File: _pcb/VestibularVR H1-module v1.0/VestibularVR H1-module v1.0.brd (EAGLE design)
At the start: 43 x 56.5 mm, 70 parts, among them IC1 FT232RL, IC2 74LVC1G07DBV, IC3 TLV70033DDCR, IC4 74LVC1G07DBV, IC5 74LVC1G07DBV, IC6 74LVC1G07DBV, IC7 USBLC6-2SC6, IC8 ATXMEGA32A4U, X1 TSW-105-02-S-D, X2 TSW-105-02-S-D, X7 22-23-2051

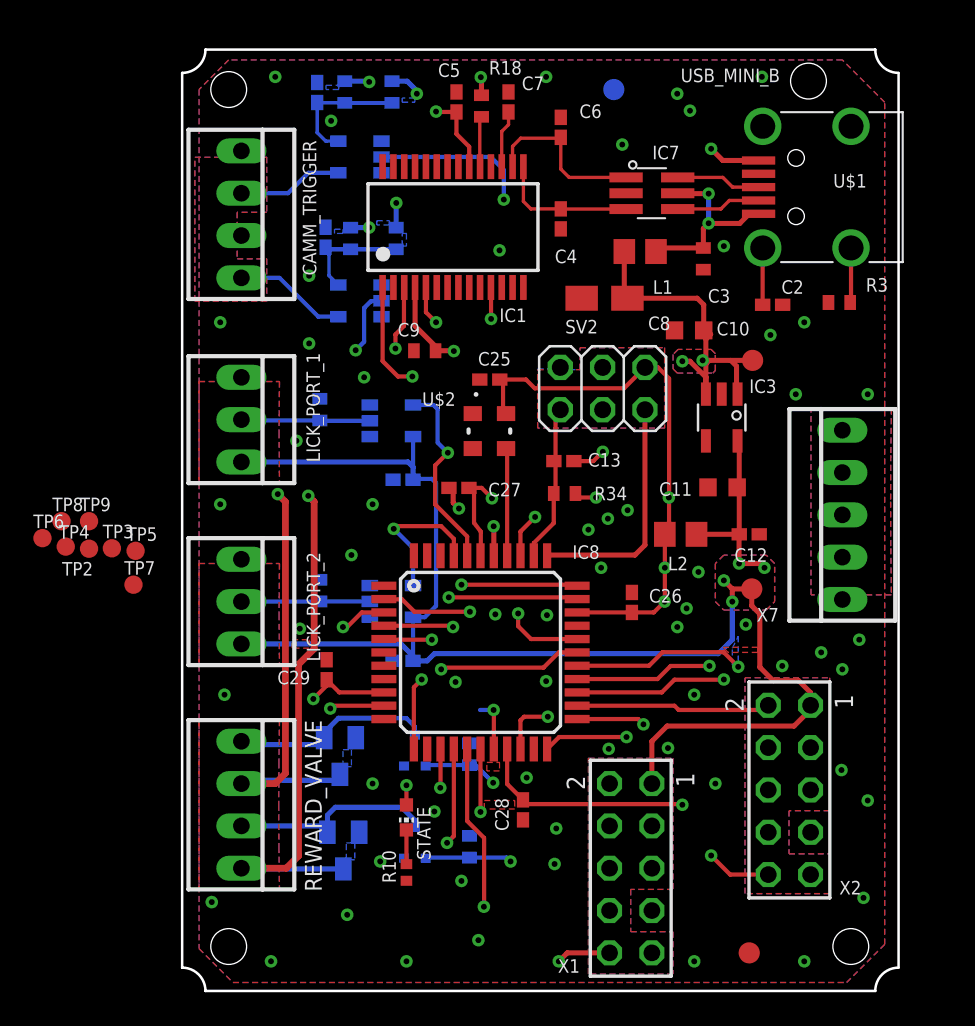
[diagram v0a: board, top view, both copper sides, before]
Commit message: v.1.0 pcb design as finished; still missing to hear about it from Filipe
. David's pcb v.1.0 design as finished
  - mechanical holes final tuning
  - main labels final design
. still missing to hear about it from Filipe
. next step - building BOM
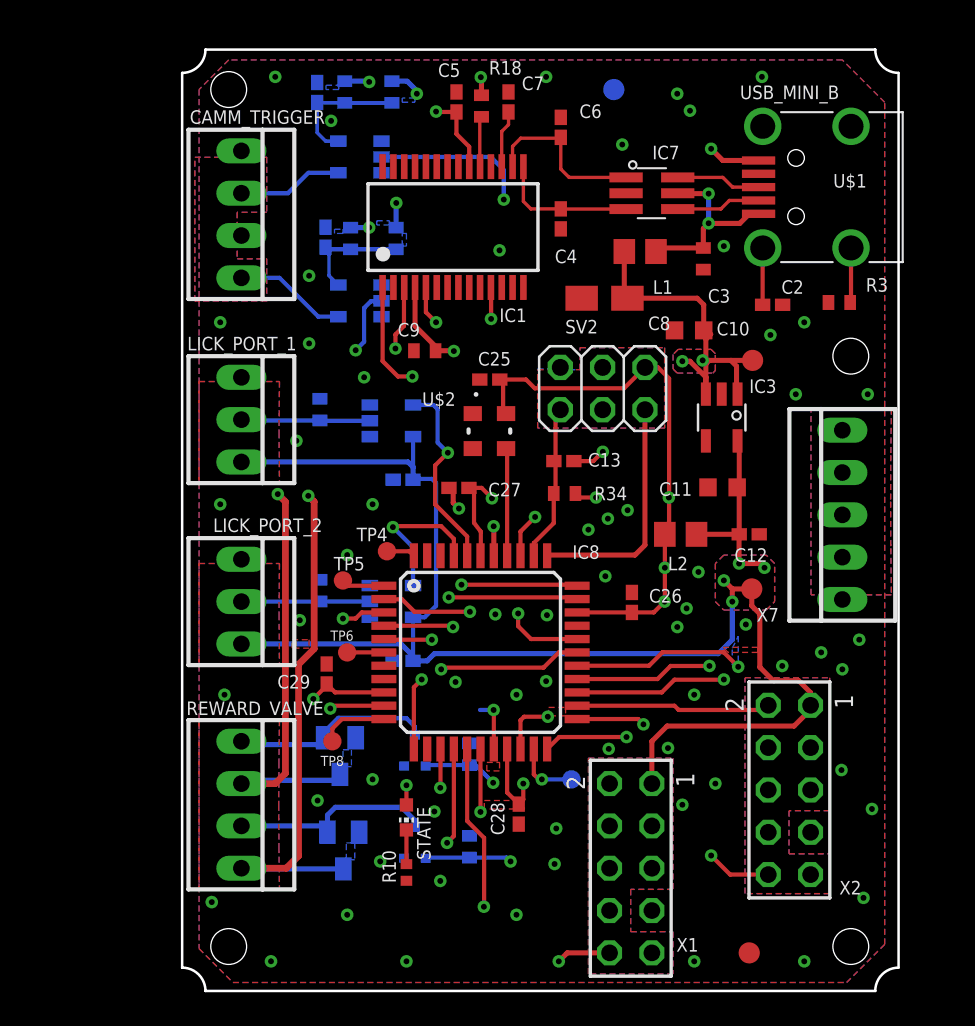
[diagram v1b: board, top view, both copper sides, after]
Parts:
- removed TP2, TP3, TP7: WIREPADSMD1,27-254, testpad:TP11R
- moved TP9 32.8 mm to (23.4, 12.7), flipped to the bottom
- moved TP8 20.9 mm to (9.02, 15.0)
- moved TP6 19.5 mm to (9.91, 20.3)
- moved TP4 17.9 mm to (12.3, 26.4)
- moved TP5 12.6 mm to (9.65, 24.6)
- moved C28 0.36 mm to (20.2, 10.6)
- moved C29 0.25 mm to (8.68, 19.0)
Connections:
- removed net N$10: IC8.43, TP3.TP
- removed net N$15: IC8.7, TP7.TP
- removed net N$8: IC8.42, TP2.TP
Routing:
- net N$17: track 0.00 -> 4.09 mm
- net N$18: track 0.00 -> 3.91 mm, vias 0 -> 1
- net +3V3_U: track 113.5 -> 110.9 mm, vias 8 -> 10
- net N$12: track 0.00 -> 2.59 mm
- net N$13: track 0.00 -> 2.20 mm
- net N$11: track 0.00 -> 1.73 mm
- net U_OPTICAL_FLOW_2_INT: track 43.8 -> 44.4 mm
- added copper zone on layer 1, net N$15

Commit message: final versions committed & CAM data
VestibularVR H1-module v1.0
  &
Lick Sensor module v1.0
final versions committed !!!

.created CAM data for both boards
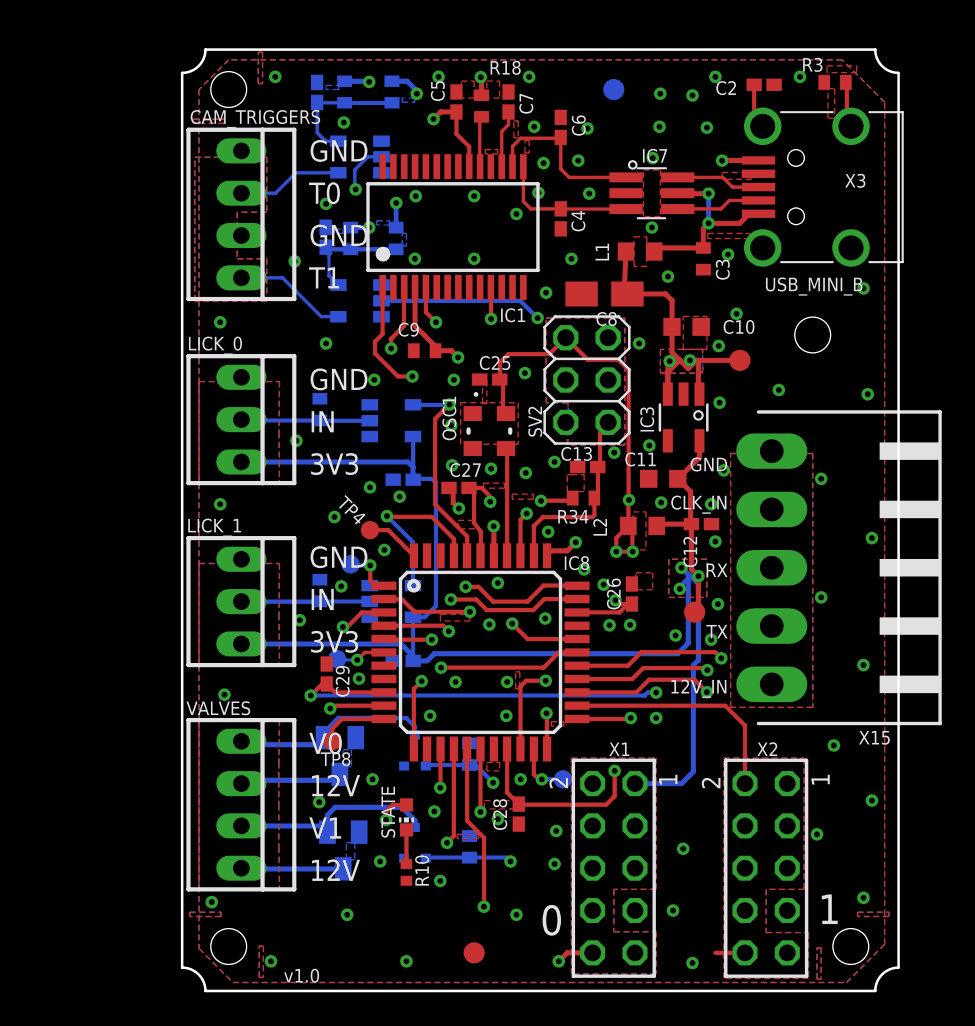
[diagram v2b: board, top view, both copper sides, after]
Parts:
- removed X7: 22-23-2051, con-molex:22-23-2051
- added X15: (no value), con-weidmueller-sl35:90G-5
- L1, L2: device rcl:R0805 -> rcl:R0603
- moved TP10 16.5 mm to (17.5, 2.29)
- moved C2 13.2 mm to (34.9, 54.4)
- moved R3 13.2 mm to (39.2, 54.5)
- moved X2 4.90 mm to (35.1, 7.37)
- moved TP1 3.70 mm to (30.8, 22.7)
- moved C11 3.59 mm to (28.9, 30.7)
- moved C12 2.93 mm to (31.2, 28.0)
- moved L2 2.34 mm to (27.6, 27.9)
- moved IC3 2.29 mm to (30.1, 34.4)
- moved TP4 1.63 mm to (11.3, 27.7)
- moved C13 1.48 mm to (24.3, 31.4), turned to 180 degrees
- moved R34 1.17 mm to (24.1, 29.6), turned to 180 degrees
- moved SV2 1.07 mm to (24.3, 36.7), turned to 90 degrees
- moved TP5 1.07 mm to (10.1, 25.6), flipped to the bottom
- moved X1 1.02 mm to (25.9, 7.37)
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- renumbered CAMM_TRIGGER to CAM_TRIGGERS, LICK_PORT_1 to LICK_0, LICK_PORT_2 to LICK_1, REWARD_VALVE to VALVES, U$1 to X3, U$2 to OSC1, U$4 to T2, U$7 to T1
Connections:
- removed net N$59: C2.1, X3.SHIELD_4
- new net N$15: C2.1, X3.SHIELD_3
- net +12V: now also X15.1; no longer X7.5
- net GND: now also X15.5; no longer X7.1
- net HARP_H1_BOARD_RX: now also X15.3; no longer X7.3
- net HARP_H1_BOARD_TX: now also X15.2; no longer X7.4
- net HARP_H1_CLOCK_IN: now also X15.4; no longer X7.2
- net N$1: now also X3.SHIELD_2; no longer X3.SHIELD_1
- net U_CAM1_TRIGGER: now also IC4.2; no longer IC2.2
- net U_CAM2_TRIGGER: now also IC2.2; no longer IC4.2
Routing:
- net +12V: track 127.5 -> 87.6 mm, vias 2 -> 0
- net HARP_H1_BOARD_TX: track 31.2 -> 17.7 mm
- net HARP_H1_BOARD_RX: track 33.1 -> 23.7 mm
- net GND: track 18.7 -> 9.47 mm, vias 55 -> 96
- net U_CAM1_TRIGGER: track 29.4 -> 38.3 mm
- net +3V3: track 209.5 -> 200.7 mm, vias 10 -> 9
- net U_OPTICAL_FLOW_2_INT: track 44.4 -> 36.7 mm
- net U_CAM2_TRIGGER: track 45.6 -> 38.0 mm
- net U_OPTICAL_FLOW_2_MISO: track 20.5 -> 24.5 mm
- net U_OPTICAL_FLOW_2_SCK: track 18.6 -> 22.0 mm
- net N$59: track 3.41 -> 0.00 mm
- net U_OPTICAL_FLOW_2_MOSI: track 15.4 -> 18.3 mm
- net N$15: track 0.00 -> 2.71 mm
- net +3V3_U: track 110.9 -> 108.3 mm, vias 10 -> 9
- net PDI_CLK: track 9.51 -> 12.1 mm
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- added copper zone on layer 1, net N$10
- added copper zone on layer 15, net N$100
- added copper zone on layer 1, net N$101
- added copper zone on layer 1, net N$102
- added copper zone on layer 2, net N$103
- added copper zone on layer 15, net N$104
- added copper zone on layer 16, net N$105
- added copper zone on layer 1, net N$106
- added copper zone on layer 1, net N$107
- added copper zone on layer 1, net N$108
- added copper zone on layer 15, net N$109
- added copper zone on layer 15, net N$110
- added copper zone on layer 15, net N$111
- added copper zone on layer 1, net N$16
- added copper zone on layer 1, net N$24
- added copper zone on layer 1, net N$25
- added copper zone on layer 1, net N$26
- added copper zone on layer 1, net N$27
- added copper zone on layer 1, net N$45
- added copper zone on layer 1, net N$47
- added copper zone on layer 1, net N$48
- added copper zone on layer 1, net N$55
- added copper zone on layer 1, net N$57
- added copper zone on layer 1, net N$59
- added copper zone on layer 1, net N$69
- added copper zone on layer 1, net N$7
- added copper zone on layer 1, net N$70
- added copper zone on layer 1, net N$71
- added copper zone on layer 2, net N$72
- added copper zone on layer 15, net N$73
- added copper zone on layer 16, net N$74
- added copper zone on layer 1, net N$75
- added copper zone on layer 1, net N$76
- added copper zone on layer 1, net N$77
- added copper zone on layer 15, net N$78
- added copper zone on layer 2, net N$79
- added copper zone on layer 15, net N$80
- added copper zone on layer 16, net N$81
- added copper zone on layer 1, net N$82
- added copper zone on layer 2, net N$83
- added copper zone on layer 15, net N$84
- added copper zone on layer 16, net N$85
- added copper zone on layer 1, net N$86
- added copper zone on layer 2, net N$87
- added copper zone on layer 15, net N$88
- added copper zone on layer 16, net N$89
- added copper zone on layer 1, net N$90
- added copper zone on layer 2, net N$91
- added copper zone on layer 15, net N$92
- added copper zone on layer 16, net N$93
- added copper zone on layer 1, net N$94
- added copper zone on layer 2, net N$95
- added copper zone on layer 15, net N$96
- added copper zone on layer 16, net N$97
- added copper zone on layer 15, net N$98
- added copper zone on layer 15, net N$99
- removed copper zone on layer 1, net N$15
- removed copper zone on layer 2, net N$45
- removed copper zone on layer 15, net N$47
- removed copper zone on layer 16, net N$48
- removed copper zone on layer 2, net N$55
- removed copper zone on layer 16, net N$57
- removed copper zone on layer 2, net N$69
- removed copper zone on layer 2, net N$7
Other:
- board text added: "0"
- board text added: "1"
- board text added: "12V"
- board text added: "12V_IN"
- board text added: "3V3"
- board text added: "CLK_IN"
- board text added: "GND"
- board text added: "IN"
- board text added: "RX"
- board text added: "T0"
- board text added: "T1"
- board text added: "TX"
- board text added: "V0"
- board text added: "V1"
- board text added: "v1.0"
- board text removed: "Vestibular VR H1 Module"

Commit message: tunings on last versions
tunings on last versions:
  - labels size & positions
  - VestibularVR H1 module get 1mm more height
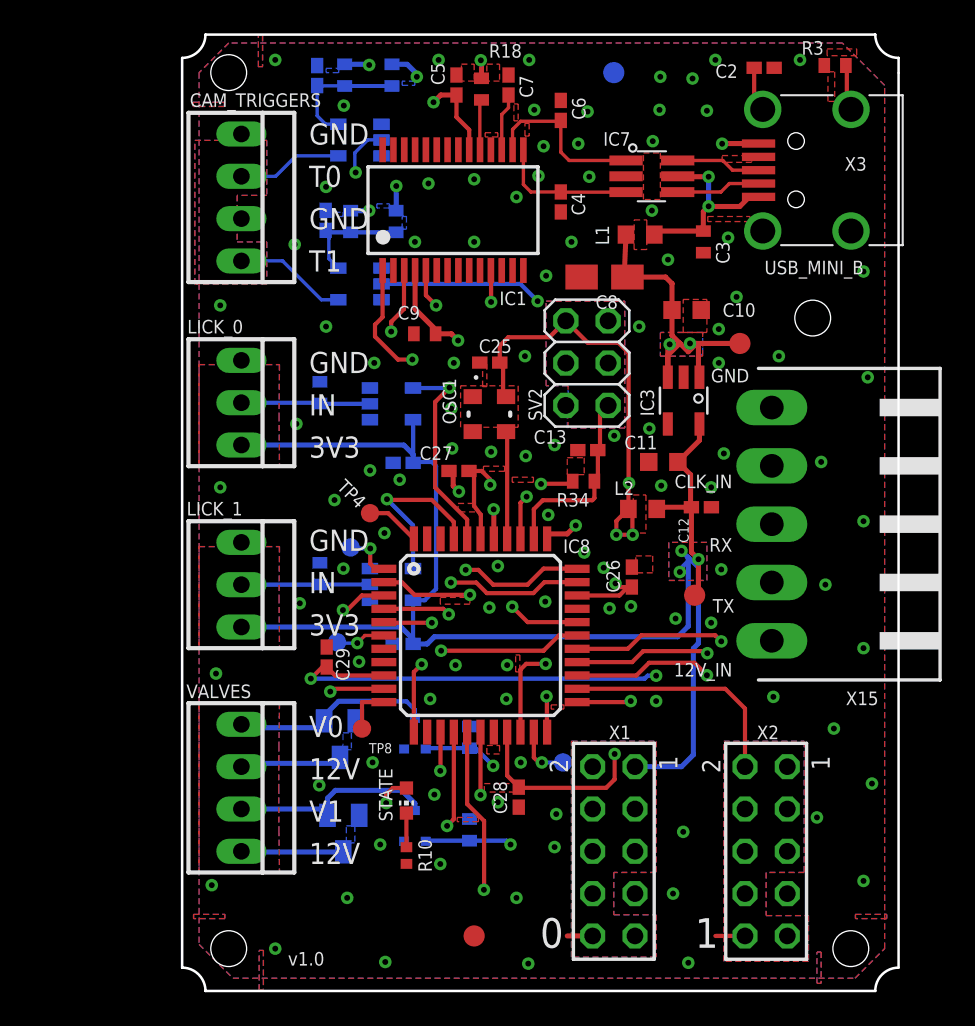
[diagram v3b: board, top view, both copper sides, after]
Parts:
- moved X15 2.62 mm to (40.6, 28.0)
- moved TP8 1.93 mm to (10.8, 15.7)
- moved C25 1.02 mm to (18.5, 37.7)
- moved C3 1.02 mm to (31.3, 45.0)
- moved IC4 1.02 mm to (10.7, 51.1)
- moved IC7 1.02 mm to (28.2, 48.9)
- moved L1 1.02 mm to (27.5, 45.4)
- moved R9 1.02 mm to (8.27, 35.9)
- moved TP11 1.02 mm to (25.9, 55.1)
- moved TP13 1.02 mm to (33.5, 38.9)
- moved X3 1.02 mm to (43.2, 49.3)
- moved C27 1.02 mm to (16.6, 31.2)
- moved C29 1.02 mm to (8.68, 20.0)
- moved IC5 1.02 mm to (12.6, 24.4)
- moved LICK_1 1.02 mm to (3.56, 24.4)
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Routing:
- net +12V: track 87.6 -> 90.7 mm
- net N$17: track 4.09 -> 2.90 mm
- net GND: track 9.47 -> 8.75 mm
- net +3V3: track 200.7 -> 200.1 mm
- added copper zone on layer 2, net N$102
- removed copper zone on layer 1, net N$102
- removed copper zone on layer 2, net N$103
- removed copper zone on layer 15, net N$104
- removed copper zone on layer 16, net N$105
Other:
- board size 43 x 56.5 mm -> 43 x 57.4 mm

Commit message: BOMs building
. BOMs building:
  - for both projects - Lick Sensor Module v1.0 & VestibularVR H1 Module v1.0
  - schm files modified (components parameters updated)

. Removed old Auxiliary Designs
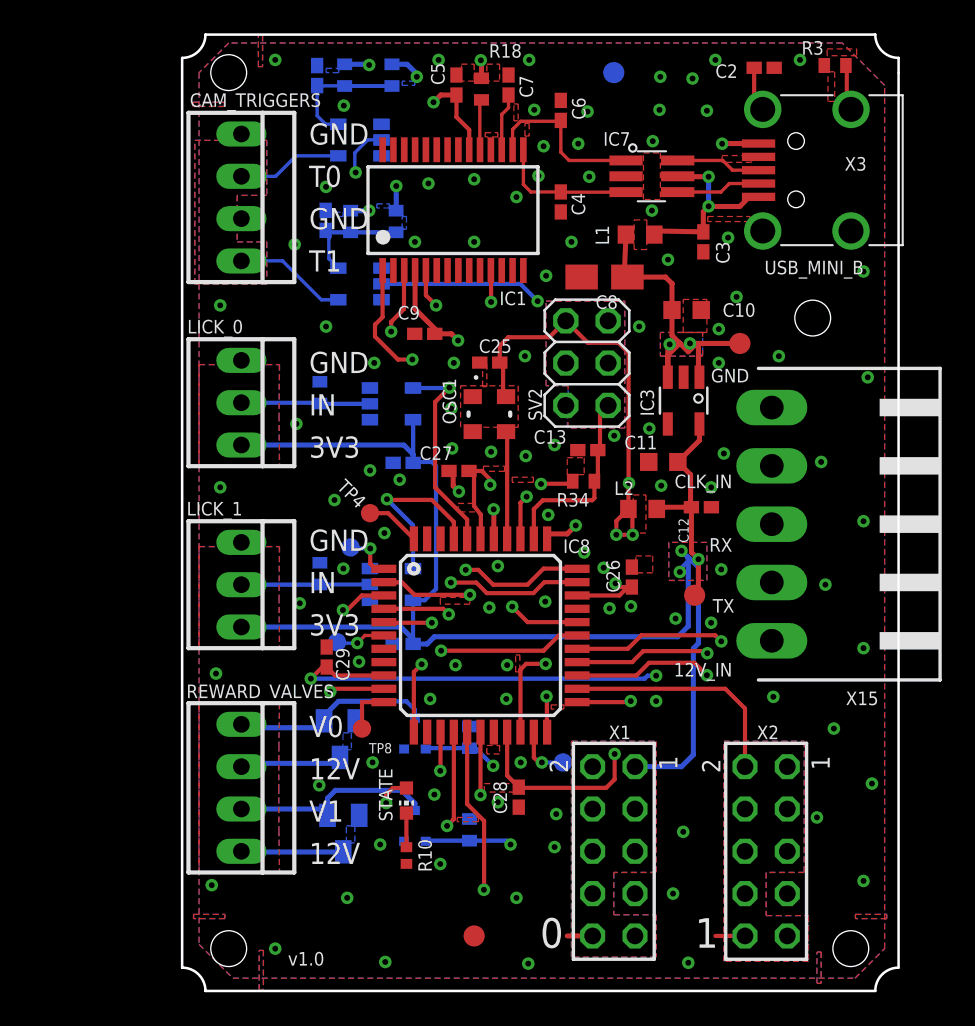
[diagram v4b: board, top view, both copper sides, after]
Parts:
- C3, C9: device rcl:C0402 -> rcl:C0402K
- R1, R5: value 0R DNI -> 0R
- R10: value 910 -> 330R
- R2, R6: value 0R DNI -> DNI
- STATE: value (none) -> GREEN_LED
- TP1, TP10, TP11, TP13: value TPB1,27 -> NO_COMPONENT
- TP4, TP5, TP6, TP8, TP9: value WIREPADSMD1,27-254 -> NO_COMPONENT
- X15: value (none) -> Main_plug
- renumbered VALVES to REWARD_VALVES

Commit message: BOM being updated
BOM being updated
not yet finished
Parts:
- C8: device rcl:A/3216-18R -> rcl:C0603
- IC3: value TLV70033DDCR -> LP5907MFX-3.3
- R8, R9: value 10k -> 1M
- moved C8 0.20 mm to (25.5, 42.8), turned to 180 degrees
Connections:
- net +5V: now also C8.1; no longer C8.+
- net GND: now also C8.2; no longer C8.-

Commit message: BOMs & start Harp Motor device H2-module v1.0
. almost final BOMs versions for VestibularVR H1-module v1.0 & Lick Sensor module v1.0
. start of new project Harp Motor device H2-module v1.0
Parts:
- CAM_TRIGGERS, REWARD_VALVES: value 22-23-2041 -> 1x4 case
- LICK_0, LICK_1: value 22-23-2031 -> 1x3 case
- X1, X2: value TSW-105-02-S-D -> 2x5 header
